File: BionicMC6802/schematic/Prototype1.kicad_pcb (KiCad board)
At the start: 2 copper layers, 95 x 72 mm, 19 parts, among them J1 Conn_AVR_UPDI, J3 Conn_I2C_Master, SW1 TSD1265, U1 ATmega4809-P, U2 HM628128DLP-5, U3 Z84C00

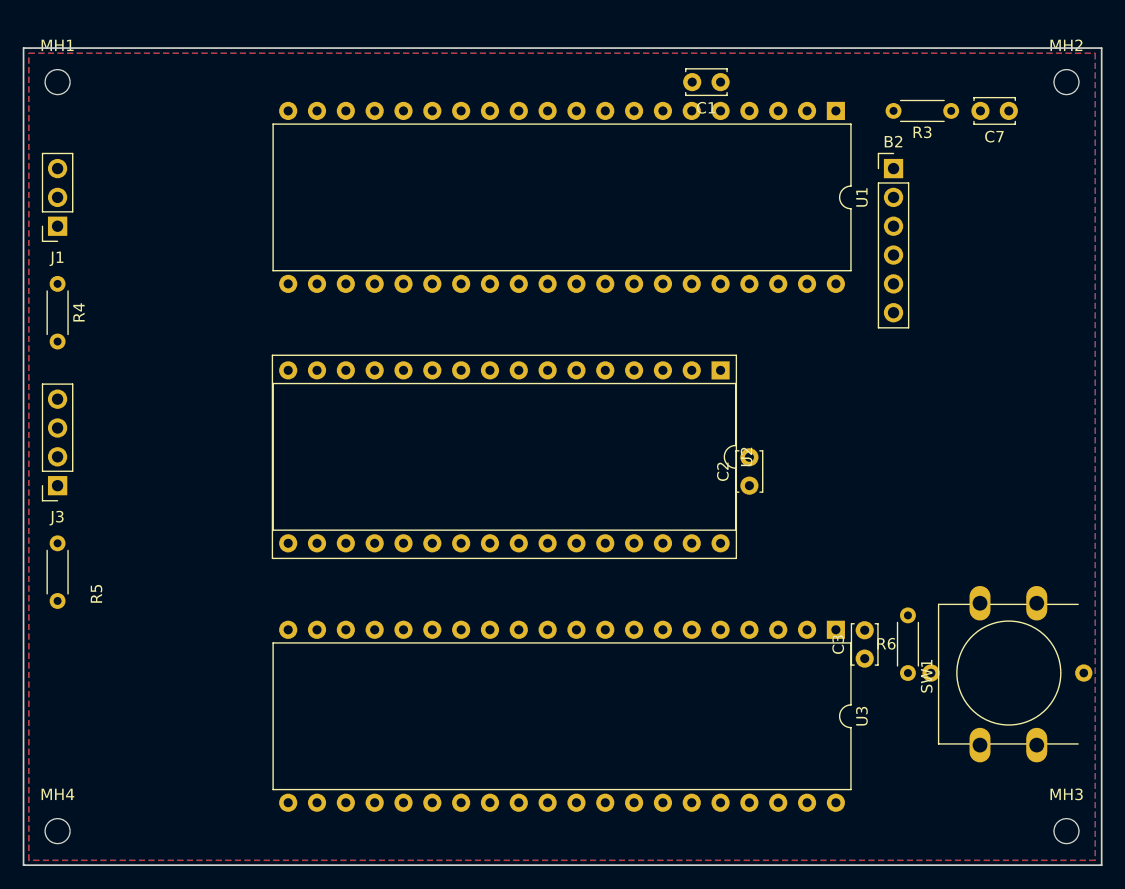
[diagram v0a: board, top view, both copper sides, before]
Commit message: [BionicMC6802] Update to BionicBase/Teensy35 configuration
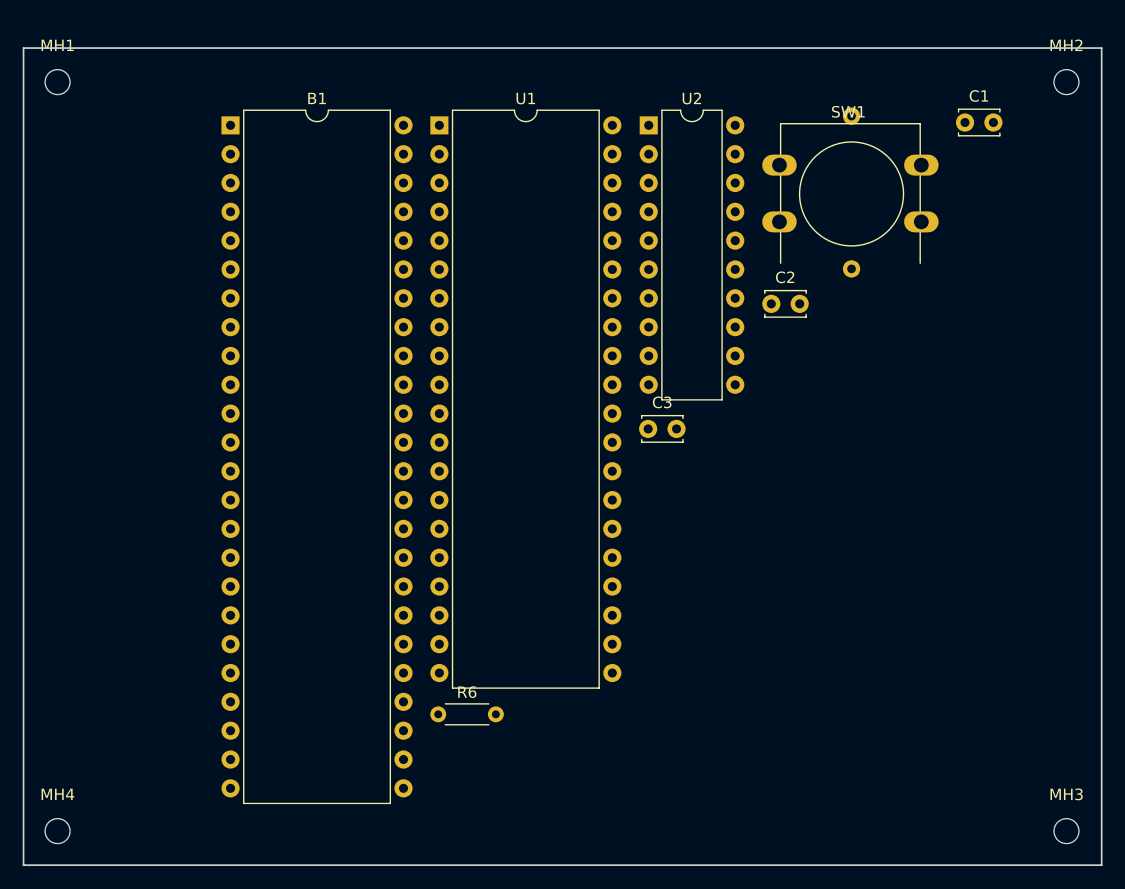
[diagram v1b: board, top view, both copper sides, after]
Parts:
- removed B2: USB_Serial, 0-LocalLibrary:GY232V2
- removed C7: 0.1u, Capacitor_THT:C_Disc_D3.4mm_W2.1mm_P2.50mm
- removed J1: Conn_AVR_UPDI, Connector_PinSocket_2.54mm:PinSocket_1x03_P2.54mm_Vertical
- removed J3: Conn_I2C_Master, Connector_PinSocket_2.54mm:PinSocket_1x04_P2.54mm_Vertical
- removed R3: 10k, Resistor_THT:R_Axial_DIN0204_L3.6mm_D1.6mm_P5.08mm_Horizontal
- removed R4, R5: 4k7, Resistor_THT:R_Axial_DIN0204_L3.6mm_D1.6mm_P5.08mm_Horizontal
- removed U3: Z84C00, Package_DIP:DIP-40_W15.24mm
- added B1: Teensy3.5, Package_DIP:DIP-48_W15.24mm, F.Cu at (116.2, 73.8)
- U1: value ATmega4809-P -> MC6802P
- U2: value HM628128DLP-5 -> 74HCT541; footprint Package_DIP:DIP-32_W15.24mm_Socket -> Package_DIP:DIP-20_W7.62mm
- moved SW1 54.1 mm to (164.6, 77.3), turned to 0 degrees
- moved R6 41.5 mm to (134.5, 125.7), turned to 0 degrees
- moved U1 35.0 mm to (134.6, 73.8), turned to 0 degrees
- moved C3 27.8 mm to (153.0, 100.6), turned to 0 degrees
- moved U2 22.5 mm to (153.1, 73.8), turned to 0 degrees
- moved C1 21.8 mm to (181.0, 73.6), turned to 0 degrees
- moved C2 16.1 mm to (163.9, 89.5), turned to 0 degrees
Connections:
- U1 pad 1: /DBG_RX -> GND
- U1 pad 10: /D1 -> /A1
- U1 pad 11: /D2 -> /A2
- U1 pad 12: /D3 -> /A3
- U1 pad 13: /D4 -> /A4
- U1 pad 14: /D5 -> /A5
- U1 pad 15: /D6 -> /A6
- U1 pad 16: /D7 -> /A7
- U1 pad 17: VCC -> /A8
- U1 pad 18: GND -> /A9
- U1 pad 19: (no net) -> /A10
- U1 pad 2: /DBG_TX -> /~HALT~
- U1 pad 20: (no net) -> /A11
- U1 pad 21: (no net) -> GND
- U1 pad 22: (no net) -> /A12
- U1 pad 23: /~INT~ -> /A13
- U1 pad 24: /~NMI~ -> /A14
- U1 pad 25: /A0 -> /A15
- U1 pad 26: /A1 -> /D7
- U1 pad 27: /~RESET~ -> /D6
- U1 pad 28: /CLK -> /D5
- U1 pad 29: /~DBG_RESET~ -> /D4
- U1 pad 3: /~RAM_E~ -> /MR
- U1 pad 30: Net-(J1-Pad1) -> /D3
- U1 pad 31: VCC -> /D2
- U1 pad 32: GND -> /D1
- U1 pad 33: /~IORQ~ -> /D0
- U1 pad 34: /~MREQ~ -> /R~W~
- U1 pad 35: /~M1~ -> VCC
- U1 pad 36: /~WAIT~ -> GND
- U1 pad 37: /~RD~ -> /CLK_E
- U1 pad 38: /~WR~ -> GND
- U1 pad 39: /~BUSREQ~ -> Net-(R1-Pad1)
- U1 pad 4: /~USR_SW~ -> /~IRQ~
- U1 pad 40: /~BUSACK~ -> /~RESET~
- U1 pad 5: VCC -> /VMA
- U1 pad 6: GND -> /~NMI~
- U1 pad 7: /~USR_LED~ -> /BA
- U1 pad 8: /~DBG_RTS~ -> VCC
- U1 pad 9: /D0 -> /A0
- U2 pad 1: (no net) -> GND
- U2 pad 10: /A10 -> GND
- U2 pad 11: /A11 -> Net-(U2-Pad11)
- U2 pad 12: /A12 -> Net-(U2-Pad12)
- U2 pad 13: /D5 -> Net-(U2-Pad13)
- U2 pad 14: /D6 -> Net-(U2-Pad14)
- U2 pad 15: /D7 -> Net-(U2-Pad15)
- U2 pad 16: GND -> Net-(U2-Pad16)
- U2 pad 17: /D4 -> /~RESET~
- U2 pad 18: /D3 -> /CLK
- U2 pad 19: /D2 -> GND
- U2 pad 2: GND -> Net-(B1-Pad21)
- U2 pad 20: /D1 -> VCC
- U2 pad 3: /A3 -> Net-(B1-Pad17)
- U2 pad 4: /A4 -> GND
- U2 pad 5: /A5 -> GND
- U2 pad 6: /A6 -> GND
- U2 pad 7: /A7 -> GND
- U2 pad 8: /A8 -> GND
- U2 pad 9: /A9 -> GND
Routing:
- removed copper zone on B.Cu, net GND
- removed copper zone on F.Cu, net GND

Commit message: [BionicMC6802] Mezzanine board
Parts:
- removed B1: Teensy3.5, Package_DIP:DIP-48_W15.24mm
- removed C3: 0.1u, Capacitor_THT:C_Disc_D3.4mm_W2.1mm_P2.50mm
- removed R6: 560, Resistor_THT:R_Axial_DIN0204_L3.6mm_D1.6mm_P5.08mm_Horizontal
- removed SW1: TSD1265, 0-LocalLibrary:SW_PUSH-LED-12mm
- added J1: BionicConnector, 0-LocalLibrary:DIP-48_W10.16mm, F.Cu at (104.2, 72.8)
- MH1, MH2, MH3, MH4: value MountingHole_2.2mm_M2 -> MountingHole_3.2mm_M3; footprint MountingHole:MountingHole_2.2mm_M2 -> MountingHole:MountingHole_3.2mm_M3
- U2: value 74HCT541 -> 74HCT126; footprint Package_DIP:DIP-20_W7.62mm -> Package_DIP:DIP-14_W7.62mm
- moved U2 65.4 mm to (126.4, 133.5), turned to 90 degrees
- moved C2 59.4 mm to (121.3, 131.0), turned to 90 degrees
- moved MH3 45.7 mm to (144.2, 136.0)
- moved MH2 45.7 mm to (144.2, 70.0)
- moved C1 40.4 mm to (144.2, 90.3), turned to 270 degrees
- moved U1 8.34 mm to (126.4, 72.5)
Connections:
- U1 pad 10: /A1 -> /P21
- U1 pad 11: /A2 -> /P22
- U1 pad 12: /A3 -> /P23
- U1 pad 13: /A4 -> /P24
- U1 pad 14: /A5 -> /P25
- U1 pad 15: /A6 -> /P26
- U1 pad 16: /A7 -> /P27
- U1 pad 17: /A8 -> /P30
- U1 pad 18: /A9 -> /P31
- U1 pad 19: /A10 -> /P32
- U1 pad 2: /~HALT~ -> /P40
- U1 pad 20: /A11 -> /P33
- U1 pad 22: /A12 -> /P34
- U1 pad 23: /A13 -> /P35
- U1 pad 24: /A14 -> /P36
- U1 pad 25: /A15 -> /P37
- U1 pad 26: /D7 -> /P17
- U1 pad 27: /D6 -> /P16
- U1 pad 28: /D5 -> /P15
- U1 pad 29: /D4 -> /P14
- U1 pad 3: /MR -> /P52
- U1 pad 30: /D3 -> /P13
- U1 pad 31: /D2 -> /P12
- U1 pad 32: /D1 -> /P11
- U1 pad 33: /D0 -> /P10
- U1 pad 34: /R~W~ -> /P41
- U1 pad 36: GND -> /P51
- U1 pad 37: /CLK_E -> /P47
- U1 pad 39: Net-(R1-Pad1) -> /P46
- U1 pad 4: /~IRQ~ -> /P42
- U1 pad 40: /~RESET~ -> /#RESET
- U1 pad 5: /VMA -> /P50
- U1 pad 6: /~NMI~ -> /P43
- U1 pad 7: /BA -> /P55
- U1 pad 9: /A0 -> /P20
- U2 pad 1: GND -> VCC
- U2 pad 12: Net-(U2-Pad12) -> GND
- U2 pad 13: Net-(U2-Pad13) -> GND
- U2 pad 14: Net-(U2-Pad14) -> VCC
- U2 pad 2: Net-(B1-Pad21) -> /P53
- U2 pad 3: Net-(B1-Pad17) -> /#RESET
- U2 pad 6: GND -> Net-(U2-Pad6)
- U2 pad 8: GND -> Net-(U2-Pad8)
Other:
- board size 95 x 72 mm -> 48.3 x 71.1 mm

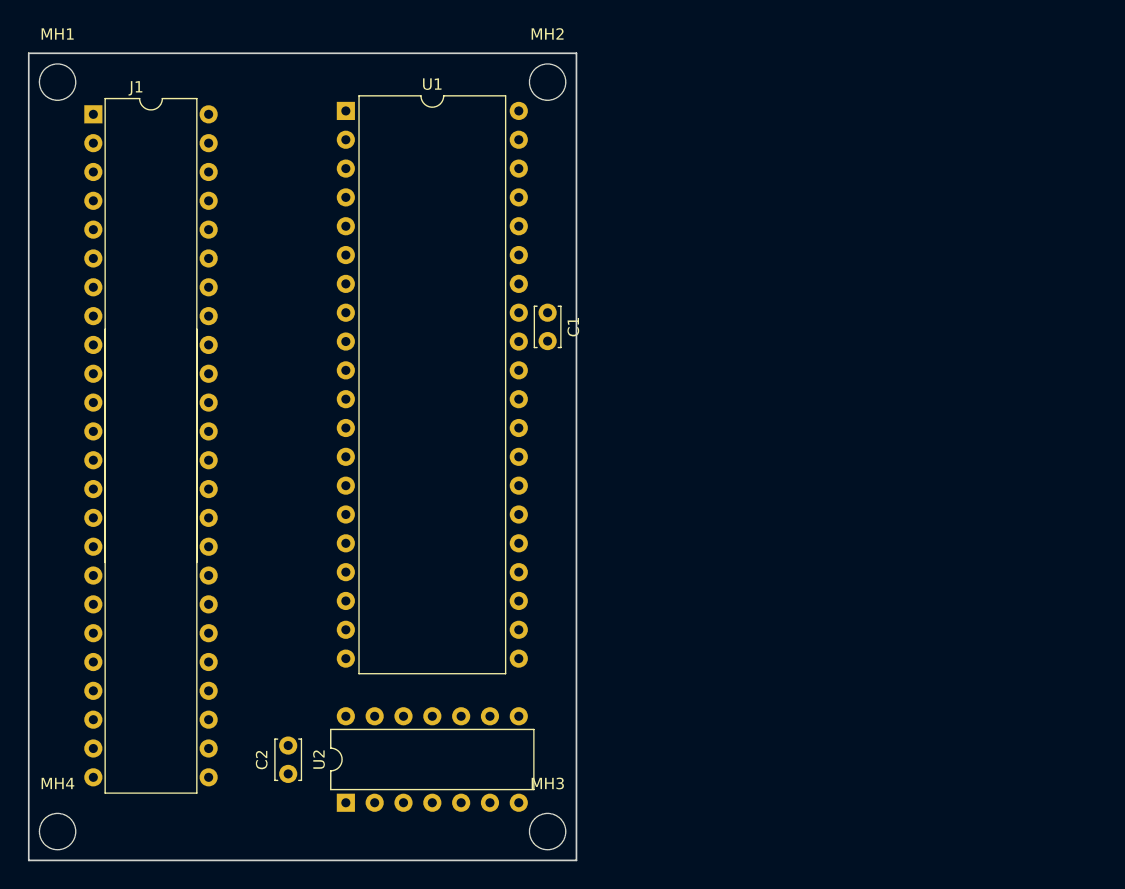
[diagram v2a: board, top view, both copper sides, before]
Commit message: [BionicMC6802] Add jumper pin to disable internal RAM
This CL also make RE pin input from the jumper pin and can switch
between MC6802 and MC6808.
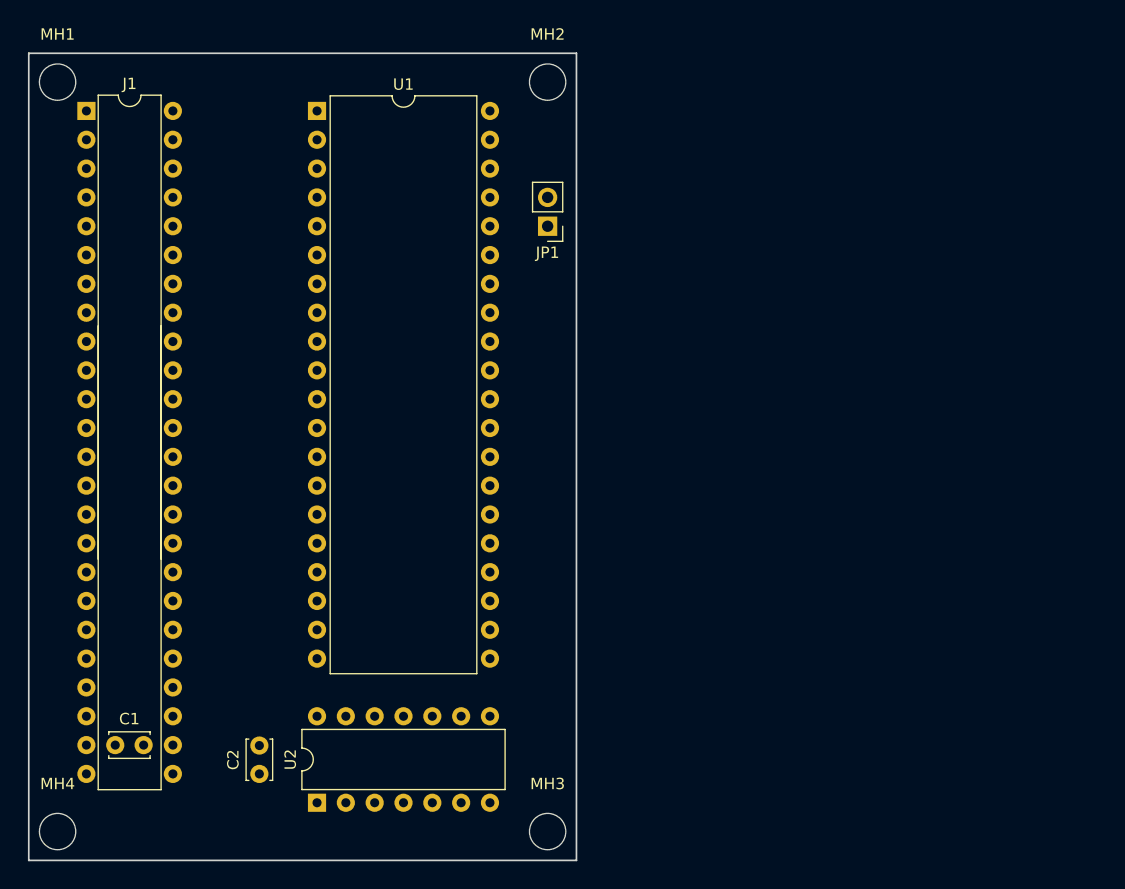
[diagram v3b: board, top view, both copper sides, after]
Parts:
- added JP1: RAM_disable, Connector_PinHeader_2.54mm:PinHeader_1x02_P2.54mm_Vertical, F.Cu at (144.2, 82.7)
- J1: footprint 0-LocalLibrary:DIP-48_W10.16mm -> 0-LocalLibrary:DIP-48_W7.62mm
- moved C1 53.9 mm to (106.1, 128.4), turned to 0 degrees
- moved U1 2.54 mm to (123.9, 72.5)
- moved U2 2.54 mm to (123.9, 133.5)
- moved C2 2.54 mm to (118.8, 131.0)
- moved J1 0.68 mm to (103.5, 72.5)
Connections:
- net /P44 renamed Net-(J1-Pad34)
- net /P45 renamed Net-(J1-Pad33)
- J1 pad 20: Net-(J1-Pad20) -> /P50
- J1 pad 21: Net-(J1-Pad21) -> /P51
- J1 pad 22: Net-(J1-Pad22) -> /P52
- J1 pad 28: Net-(J1-Pad28) -> /P55
- J1 pad 35: /P35 -> /P43
- J1 pad 40: /P36 -> /P37
- J1 pad 41: /P35 -> /P36
- J1 pad 42: /P34 -> /P35
- J1 pad 43: Net-(J1-Pad43) -> /P34
- J1 pad 44: Net-(J1-Pad44) -> /P33
- J1 pad 45: Net-(J1-Pad45) -> /P32
- J1 pad 46: Net-(J1-Pad46) -> /P31
- J1 pad 47: Net-(J1-Pad47) -> /P30

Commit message: Fix Bionic connector pin outs
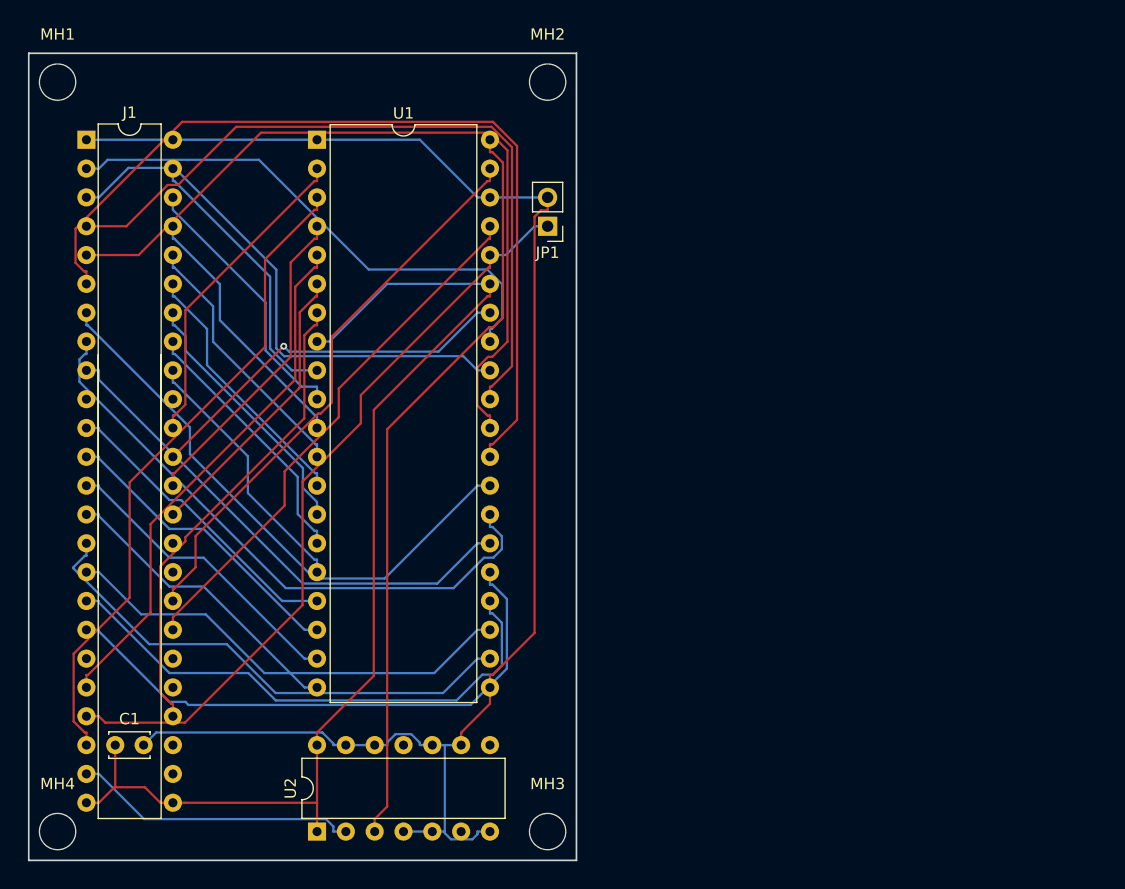
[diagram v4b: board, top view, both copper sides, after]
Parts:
- removed C2: 0.1u, Capacitor_THT:C_Disc_D3.4mm_W2.1mm_P2.50mm
- moved J1 2.54 mm to (103.5, 75.1)
- moved U1 2.54 mm to (123.9, 75.1)
- moved U2 2.54 mm to (123.9, 136.0)
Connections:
- net /#RESET renamed Net-(U1-Pad40)
- J1 pad 11: /P20 -> /P30
- J1 pad 12: /P21 -> /P31
- J1 pad 13: /P22 -> /P32
- J1 pad 14: /P23 -> /P33
- J1 pad 15: /P24 -> /P34
- J1 pad 16: /P25 -> /P35
- J1 pad 17: /P26 -> /P36
- J1 pad 18: /P27 -> /P37
- J1 pad 40: /P37 -> /P27
- J1 pad 41: /P36 -> /P26
- J1 pad 42: /P35 -> /P25
- J1 pad 43: /P34 -> /P24
- J1 pad 44: /P33 -> /P23
- J1 pad 45: /P32 -> /P22
- J1 pad 46: /P31 -> /P21
- J1 pad 47: /P30 -> /P20
- JP1 pad 1: /P50 -> /P51
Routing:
- net GND: track 0.00 -> 140.7 mm
- net VCC: track 0.00 -> 97.2 mm
- net /P14: track 0.00 -> 77.6 mm
- net /P13: track 0.00 -> 68.6 mm
- net /P51: track 0.00 -> 67.5 mm
- net Net-(U1-Pad40): track 0.00 -> 66.5 mm
- net /P12: track 0.00 -> 65.0 mm
- net /P52: track 0.00 -> 57.8 mm
- net /P16: track 0.00 -> 53.7 mm
- net /P15: track 0.00 -> 50.7 mm
- net /P37: track 0.00 -> 50.4 mm
- net /P46: track 0.00 -> 50.0 mm
- net /P11: track 0.00 -> 48.1 mm
- net /P36: track 0.00 -> 47.9 mm
- net /P47: track 0.00 -> 47.2 mm
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
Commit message: Migrate to KiCad 6.0
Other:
- net class Default removed
